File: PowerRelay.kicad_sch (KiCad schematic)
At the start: 26 parts, among them J1 Screw_Terminal_01x03, J2 Conn_01x20_Female, J3 Conn_01x20_Female, J4 Conn_01x02_Female, J5 Screw_Terminal_01x03, J6 Screw_Terminal_01x03, J7 Conn_01x02_Female, K1 G5LE-1A4_DC3, K2 G5LE-1A4_DC3, Q1 2N7000, Q2 2N7000

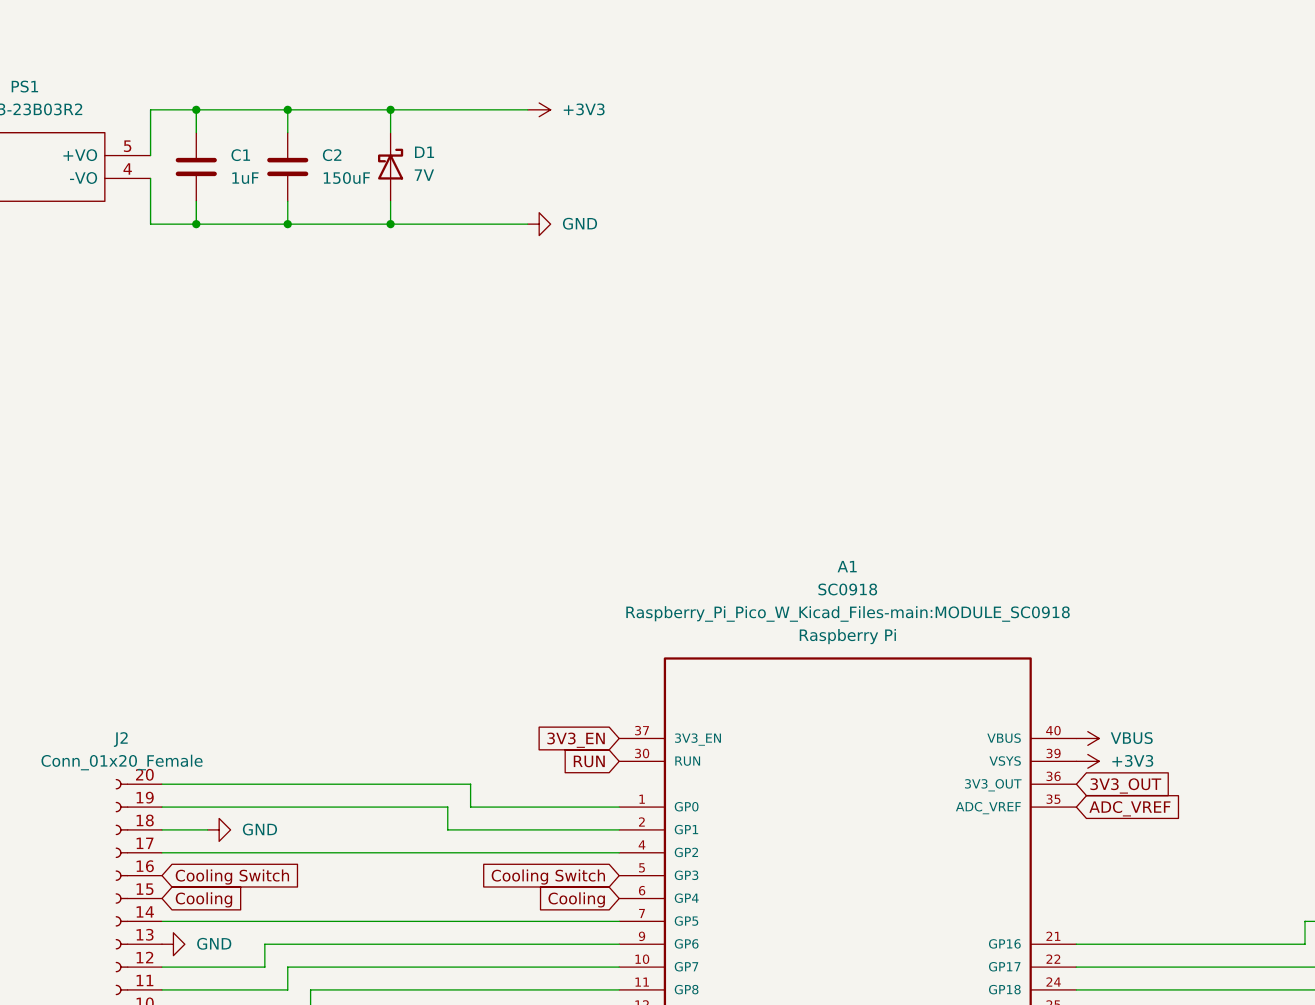
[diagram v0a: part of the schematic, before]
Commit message: add aux port for inter board comunication
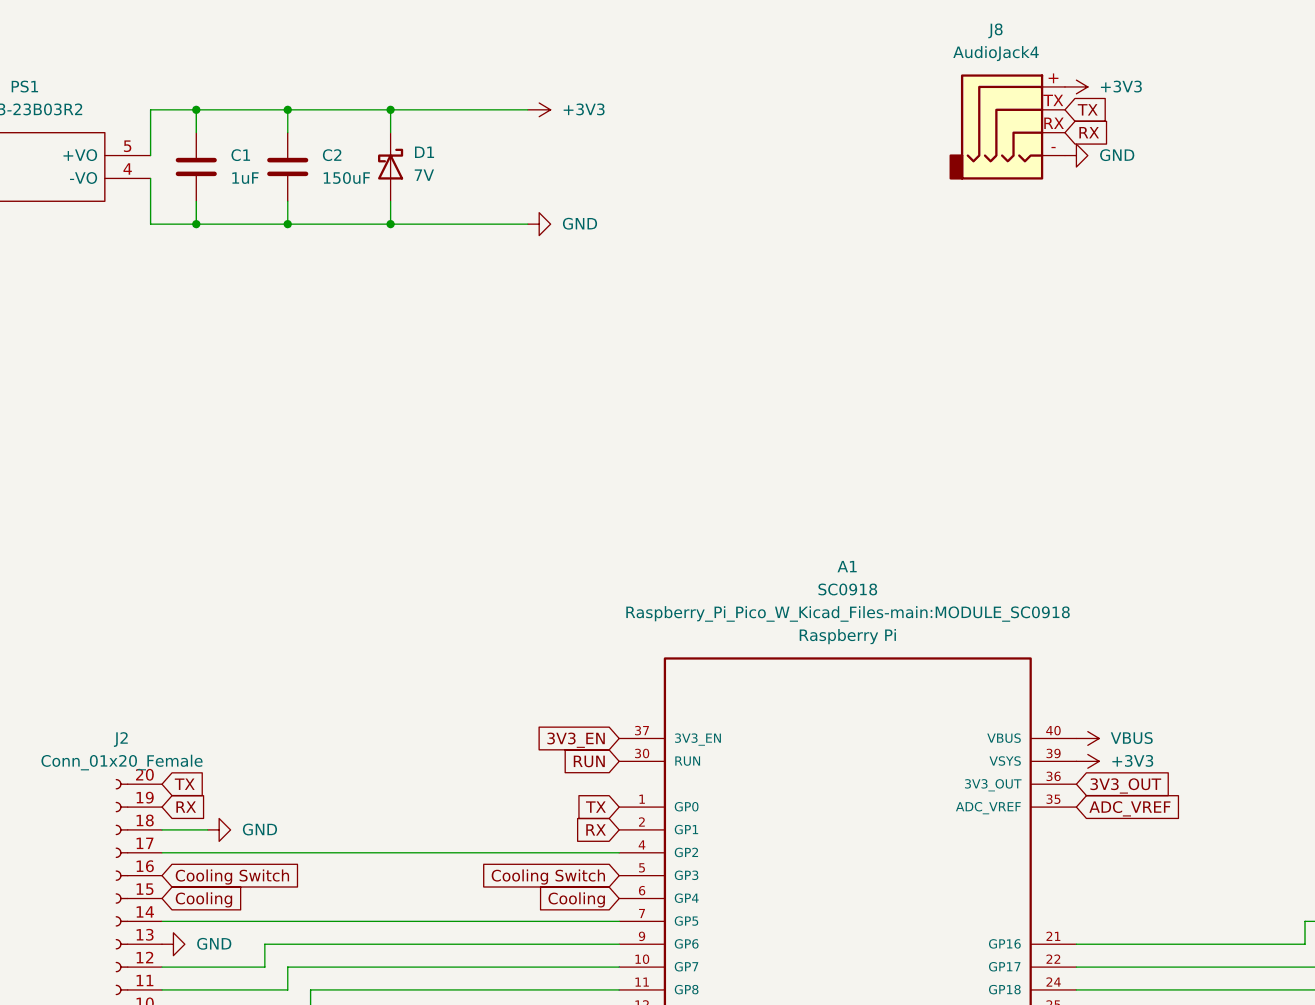
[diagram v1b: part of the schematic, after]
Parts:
- added J8: AudioJack4, 54-00174:54-00174_JACK, symbol 54-00174:54-00174
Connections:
- net +3V3: now also J8.+
- net GND: now also J8.-
- net TX: now reaches A1.1 (GP0), J2.20 (Pin_20)
- net TX: now also J8.TX
- net RX: now reaches A1.2 (GP1), J2.19 (Pin_19)
- net RX: now also J8.RX
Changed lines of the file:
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@@
-    (stroke (width 0) (type default) (color 0 0 0 0))
-  )
-  (wire (pts (xy 92.71 115.57) (xy 124.46 115.57))
     (stroke (width 0) (type default) (color 0 0 0 0))
   )
@@
     (stroke (width 0) (type default) (color 0 0 0 0))
   )
-  (wire (pts (xy 124.46 118.11) (xy 143.51 118.11))
-    (stroke (width 0) (type default) (color 0 0 0 0))
-  )
   (wire (pts (xy 91.44 45.72) (xy 91.44 50.8))
     (stroke (width 0) (type default) (color 0 0 0 0))
@@
     (stroke (width 0) (type default) (color 0 0 0 0))
   )
-  (wire (pts (xy 127 115.57) (xy 127 113.03))
-    (stroke (width 0) (type default) (color 0 0 0 0))
-  )
   (wire (pts (xy 345.44 85.09) (xy 377.19 85.09))
     (stroke (width 0) (type default) (color 0 0 0 0))
@@
     (stroke (width 0) (type default) (color 0 0 0 0))
   )
-  (wire (pts (xy 124.46 115.57) (xy 124.46 118.11))
-    (stroke (width 0) (type default) (color 0 0 0 0))
-  )
   (wire (pts (xy 96.52 48.26) (xy 96.52 50.8))
     (stroke (width 0) (type default) (color 0 0 0 0))
@@
   )
   (wire (pts (xy 96.52 38.1) (xy 96.52 40.64))
-    (stroke (width 0) (type default) (color 0 0 0 0))
-  )
-  (wire (pts (xy 143.51 115.57) (xy 127 115.57))
-    (stroke (width 0) (type default) (color 0 0 0 0))
-  )
-  (wire (pts (xy 127 113.03) (xy 92.71 113.03))
     (stroke (width 0) (type default) (color 0 0 0 0))
   )
@@
     )
   )
+  (global_label "RX" (shape input) (at 193.04 40.64 0) (fields_autoplaced)
+    (effects (font (size 1.27 1.27)) (justify left))
+    (property "Intersheet References" "${INTERSHEET_REFS}" (id 0) (at 197.9326 40.7194 0)
+      (effects (font (size 1.27 1.27)) (justify left) hide)
+    )
+  )
   (global_label "Cooling Switch" (shape input) (at 143.51 123.19 180) (fields_autoplaced)
     (effects (font (size 1.27 1.27)) (justify right))
@@
     )
   )
+  (global_label "TX" (shape input) (at 193.04 38.1 0) (fields_autoplaced)
+    (effects (font (size 1.27 1.27)) (justify left))
+    (property "Intersheet References" "${INTERSHEET_REFS}" (id 0) (at 197.6302 38.1794 0)
+      (effects (font (size 1.27 1.27)) (justify left) hide)
+    )
+  )
+  (global_label "RX" (shape input) (at 143.51 118.11 180) (fields_autoplaced)
+    (effects (font (size 1.27 1.27)) (justify right))
+    (property "Intersheet References" "${INTERSHEET_REFS}" (id 0) (at 138.6174 118.0306 0)
+      (effects (font (size 1.27 1.27)) (justify right) hide)
+    )
+  )
+  (global_label "TX" (shape input) (at 143.51 115.57 180) (fields_autoplaced)
+    (effects (font (size 1.27 1.27)) (justify right))
+    (property "Intersheet References" "${INTERSHEET_REFS}" (id 0) (at 138.9198 115.4906 0)
+      (effects (font (size 1.27 1.27)) (justify right) hide)
+    )
+  )
   (global_label "Heating" (shape input) (at 194.31 151.13 0) (fields_autoplaced)
     (effects (font (size 1.27 1.27)) (justify left))
@@
     )
   )
+  (global_label "RX" (shape input) (at 92.71 115.57 0) (fields_autoplaced)
+    (effects (font (size 1.27 1.27)) (justify left))
+    (property "Intersheet References" "${INTERSHEET_REFS}" (id 0) (at 97.6026 115.6494 0)
+      (effects (font (size 1.27 1.27)) (justify left) hide)
+    )
+  )
+  (global_label "TX" (shape input) (at 92.71 113.03 0) (fields_autoplaced)
+    (effects (font (size 1.27 1.27)) (justify left))
+    (property "Intersheet References" "${INTERSHEET_REFS}" (id 0) (at 97.3002 113.1094 0)
+      (effects (font (size 1.27 1.27)) (justify left) hide)
+    )
+  )
   (global_label "3V3_OUT" (shape input) (at 194.31 113.03 0) (fields_autoplaced)
     (effects (font (size 1.27 1.27)) (justify left))
@@
     )
   )
+  (symbol (lib_id "power:+3V3") (at 193.04 35.56 270) (unit 1)
+    (in_bom yes) (on_board yes) (fields_autoplaced)
+    (property "Reference" "#PWR0131" (id 0) (at 189.23 35.56 0)
+      (effects (font (size 1.27 1.27)) hide)
+    )
+    (property "Value" "+3V3" (id 1) (at 196.85 35.5599 90)
+      (effects (font (size 1.27 1.27)) (justify left))
+    )
+    (property "Footprint" "" (id 2) (at 193.04 35.56 0)
+      (effects (font (size 1.27 1.27)) hide)
+    )
+    (property "Datasheet" "" (id 3) (at 193.04 35.56 0)
+      (effects (font (size 1.27 1.27)) hide)
+    )
+    (pin "1")
+  )
   (symbol (lib_id "power:GND") (at 308.61 95.25 0) (unit 1)
     (in_bom yes) (on_board yes) (fields_autoplaced)
@@
     (pin "3")
     (pin "5")
+  )
+  (symbol (lib_id "54-00174:54-00174") (at 187.96 38.1 0) (unit 1)
+    (in_bom yes) (on_board yes) (fields_autoplaced)
+    (property "Reference" "J8" (id 0) (at 185.42 29.21 0))
+    (property "Value" "AudioJack4" (id 1) (at 185.42 31.75 0))
+    (property "Footprint" "54-00174:54-00174_JACK" (id 2) (at 187.96 38.1 0)
+      (effects (font (size 1.27 1.27)) hide)
+    )
+    (property "Datasheet" "~" (id 3) (at 187.96 38.1 0)
+      (effects (font (size 1.27 1.27)) hide)
+    )
+    (pin "+")
+    (pin "-")
+    (pin "RX")
+    (pin "TX")
   )
   (symbol (lib_id "power:GND") (at 308.61 66.04 0) (unit 1)
@@
     )
     (property "Datasheet" "" (id 3) (at 92.71 130.81 0)
+      (effects (font (size 1.27 1.27)) hide)
+    )
+    (pin "1")
+  )
+  (symbol (lib_id "power:GND") (at 193.04 43.18 90) (unit 1)
+    (in_bom yes) (on_board yes) (fields_autoplaced)
+    (property "Reference" "#PWR0132" (id 0) (at 199.39 43.18 0)
+      (effects (font (size 1.27 1.27)) hide)
+    )
+    (property "Value" "GND" (id 1) (at 196.85 43.1799 90)
+      (effects (font (size 1.27 1.27)) (justify right))
+    )
+    (property "Footprint" "" (id 2) (at 193.04 43.18 0)
+      (effects (font (size 1.27 1.27)) hide)
+    )
+    (property "Datasheet" "" (id 3) (at 193.04 43.18 0)
       (effects (font (size 1.27 1.27)) hide)
     )
@@
       (reference "#PWR0130") (unit 1) (value "GND") (footprint "")
     )
+    (path "/058564c8-d209-4734-add6-195b3e479042"
+      (reference "#PWR0131") (unit 1) (value "+3V3") (footprint "")
+    )
+    (path "/71ce9b05-3305-4bbf-8432-d5ad65ebcc7c"
+      (reference "#PWR0132") (unit 1) (value "GND") (footprint "")
+    )
     (path "/c87be6ab-a6c9-4fa4-8139-853165cbda8b"
       (reference "A1") (unit 1) (value "SC0918") (footprint "Raspberry_Pi_Pico_W_Kicad_Files-main:MODULE_SC0918")
@@
       (reference "J7") (unit 1) (value "Conn_01x02_Female") (footprint "Connector_PinHeader_2.54mm:PinHeader_1x02_P2.54mm_Vertical")
     )
+    (path "/0faf3218-cf03-4891-a339-737e2b007313"
+      (reference "J8") (unit 1) (value "AudioJack4") (footprint "54-00174:54-00174_JACK")
+    )
     (path "/0c60b6b1-454c-4d0f-917e-b324a07c454f"
